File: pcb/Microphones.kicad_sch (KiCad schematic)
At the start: 38 parts, among them U4 AD8426ACPZ-R7, U5 AD8426ACPZ-R7

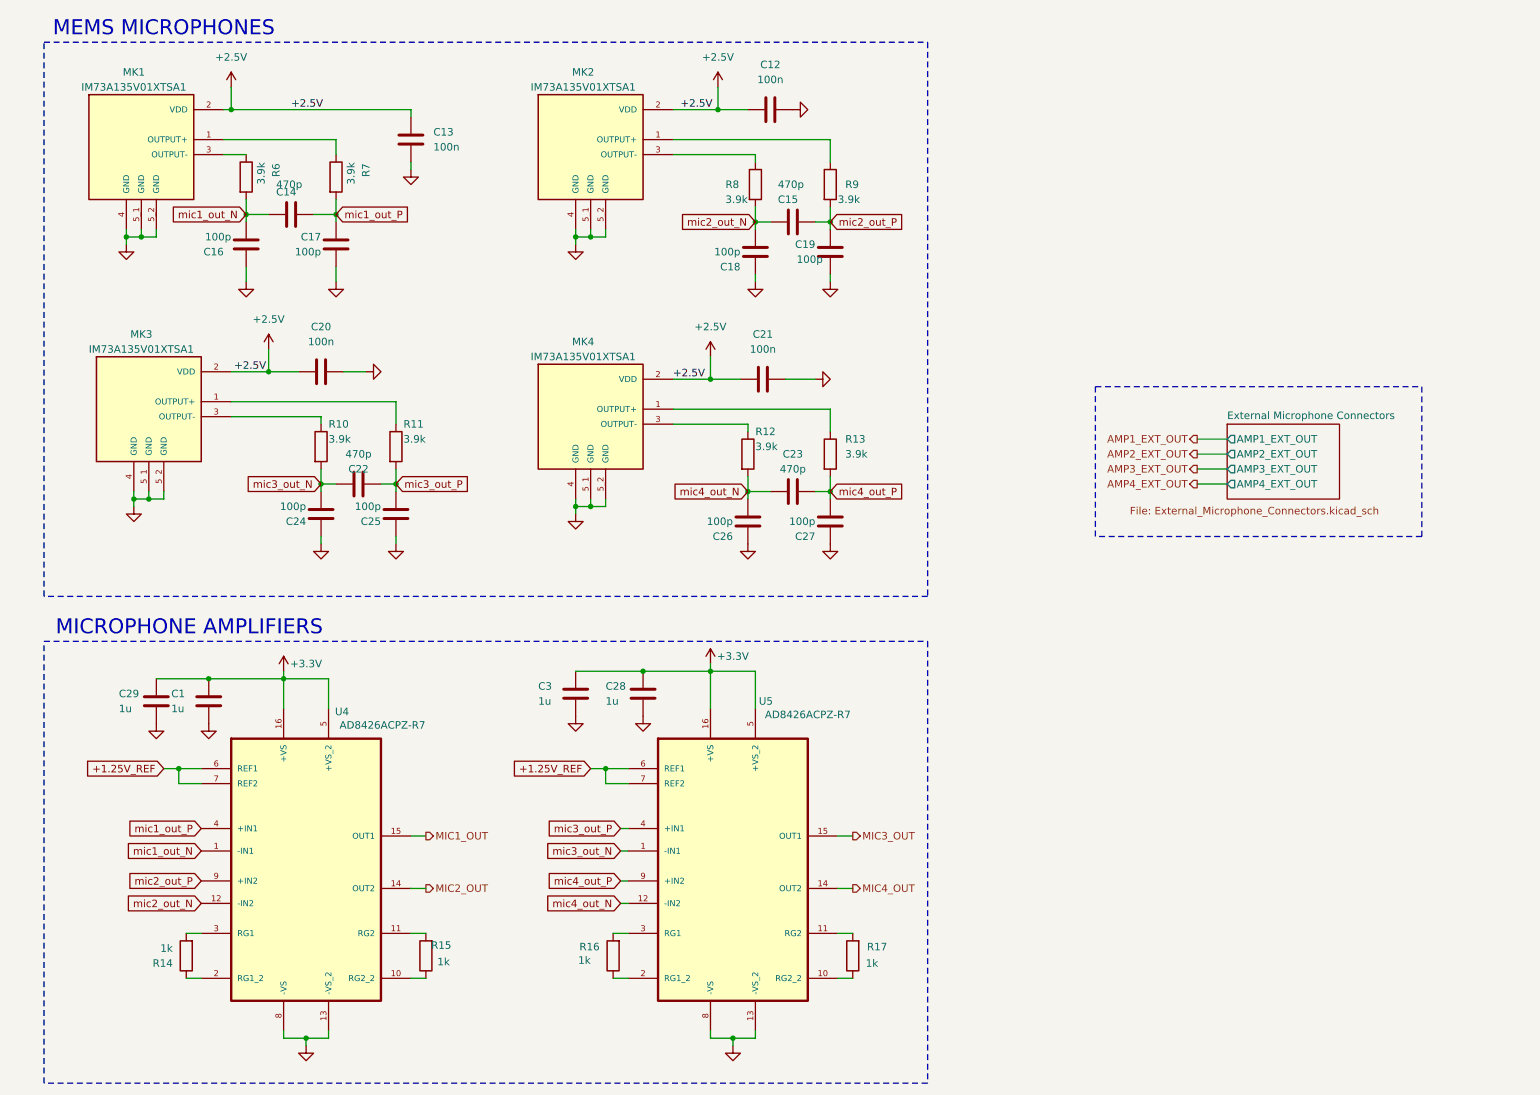
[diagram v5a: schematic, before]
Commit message: feat: Improve PCB design after tests of rev 0.8
- Added new generation of humidity sensor
- New silkscreen information for different components
- Added additional testpoints
- Removed PWM path for ultrasound transmitter
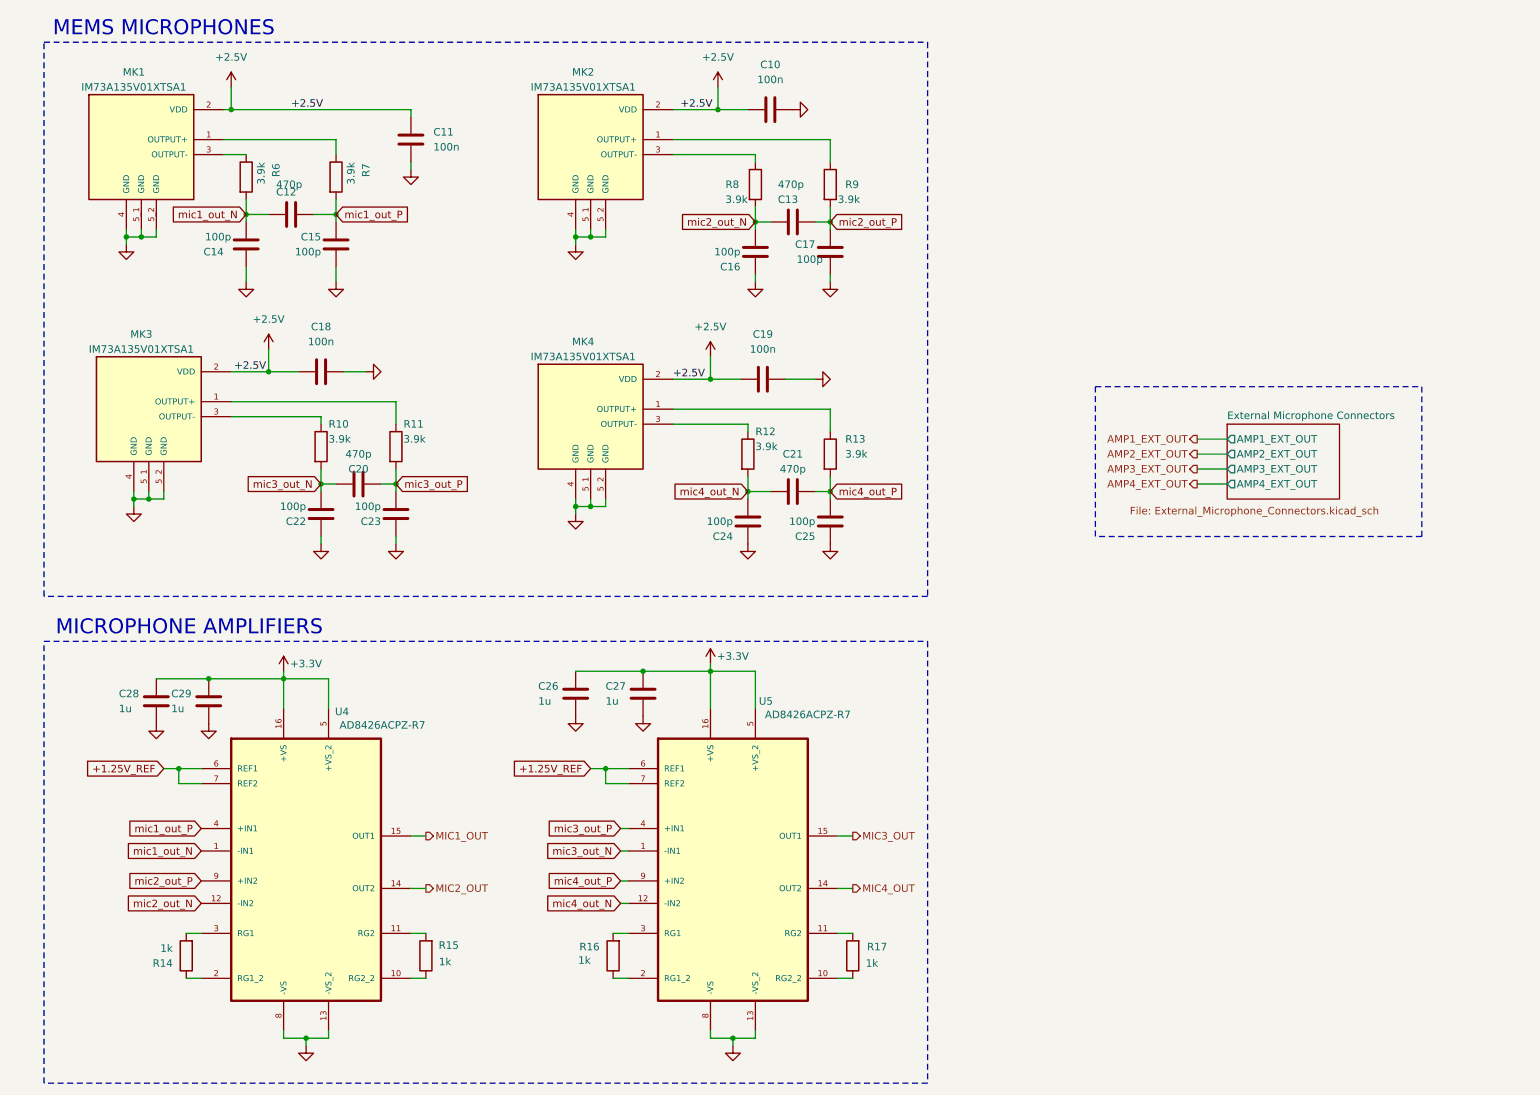
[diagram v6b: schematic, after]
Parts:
- C10: renamed from C12; footprint Capacitor_SMD:C_0603_1608Metric -> SensEdu:C_0603_1608Metric
- C11: renamed from C13; footprint Capacitor_SMD:C_0603_1608Metric -> SensEdu:C_0603_1608Metric
- C12: renamed from C14; footprint Capacitor_SMD:C_0603_1608Metric -> SensEdu:C_0603_1608Metric
- C13: renamed from C15; footprint Capacitor_SMD:C_0603_1608Metric -> SensEdu:C_0603_1608Metric
- C14: renamed from C16; footprint Capacitor_SMD:C_0603_1608Metric -> SensEdu:C_0603_1608Metric
- C15: renamed from C17; footprint Capacitor_SMD:C_0603_1608Metric -> SensEdu:C_0603_1608Metric
- C16: renamed from C18; footprint Capacitor_SMD:C_0603_1608Metric -> SensEdu:C_0603_1608Metric
- C17: renamed from C19; footprint Capacitor_SMD:C_0603_1608Metric -> SensEdu:C_0603_1608Metric
- C18: renamed from C20; footprint Capacitor_SMD:C_0603_1608Metric -> SensEdu:C_0603_1608Metric
- C19: renamed from C21; footprint Capacitor_SMD:C_0603_1608Metric -> SensEdu:C_0603_1608Metric
- C20: renamed from C22; footprint Capacitor_SMD:C_0603_1608Metric -> SensEdu:C_0603_1608Metric
- C21: renamed from C23; footprint Capacitor_SMD:C_0603_1608Metric -> SensEdu:C_0603_1608Metric
- C22: renamed from C24; footprint Capacitor_SMD:C_0603_1608Metric -> SensEdu:C_0603_1608Metric
- C23: renamed from C25; footprint Capacitor_SMD:C_0603_1608Metric -> SensEdu:C_0603_1608Metric
- C24: renamed from C26; footprint Capacitor_SMD:C_0603_1608Metric -> SensEdu:C_0603_1608Metric
- C25: renamed from C27; footprint Capacitor_SMD:C_0603_1608Metric -> SensEdu:C_0603_1608Metric
- C26: renamed from C3; footprint Capacitor_SMD:C_0603_1608Metric -> SensEdu:C_0603_1608Metric
- C27: renamed from C28; footprint Capacitor_SMD:C_0603_1608Metric -> SensEdu:C_0603_1608Metric
- C28: renamed from C29; footprint Capacitor_SMD:C_0603_1608Metric -> SensEdu:C_0603_1608Metric
- C29: renamed from C1; footprint Capacitor_SMD:C_0603_1608Metric -> SensEdu:C_0603_1608Metric
- R10, R11, R12, R13, R14, R15, R16, R17, R6, R7, R8, R9: footprint Resistor_SMD:R_0603_1608Metric -> SensEdu:R_0603_1608Metric

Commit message: refactor: Remove unnecessary comments
- Regenerate schematics
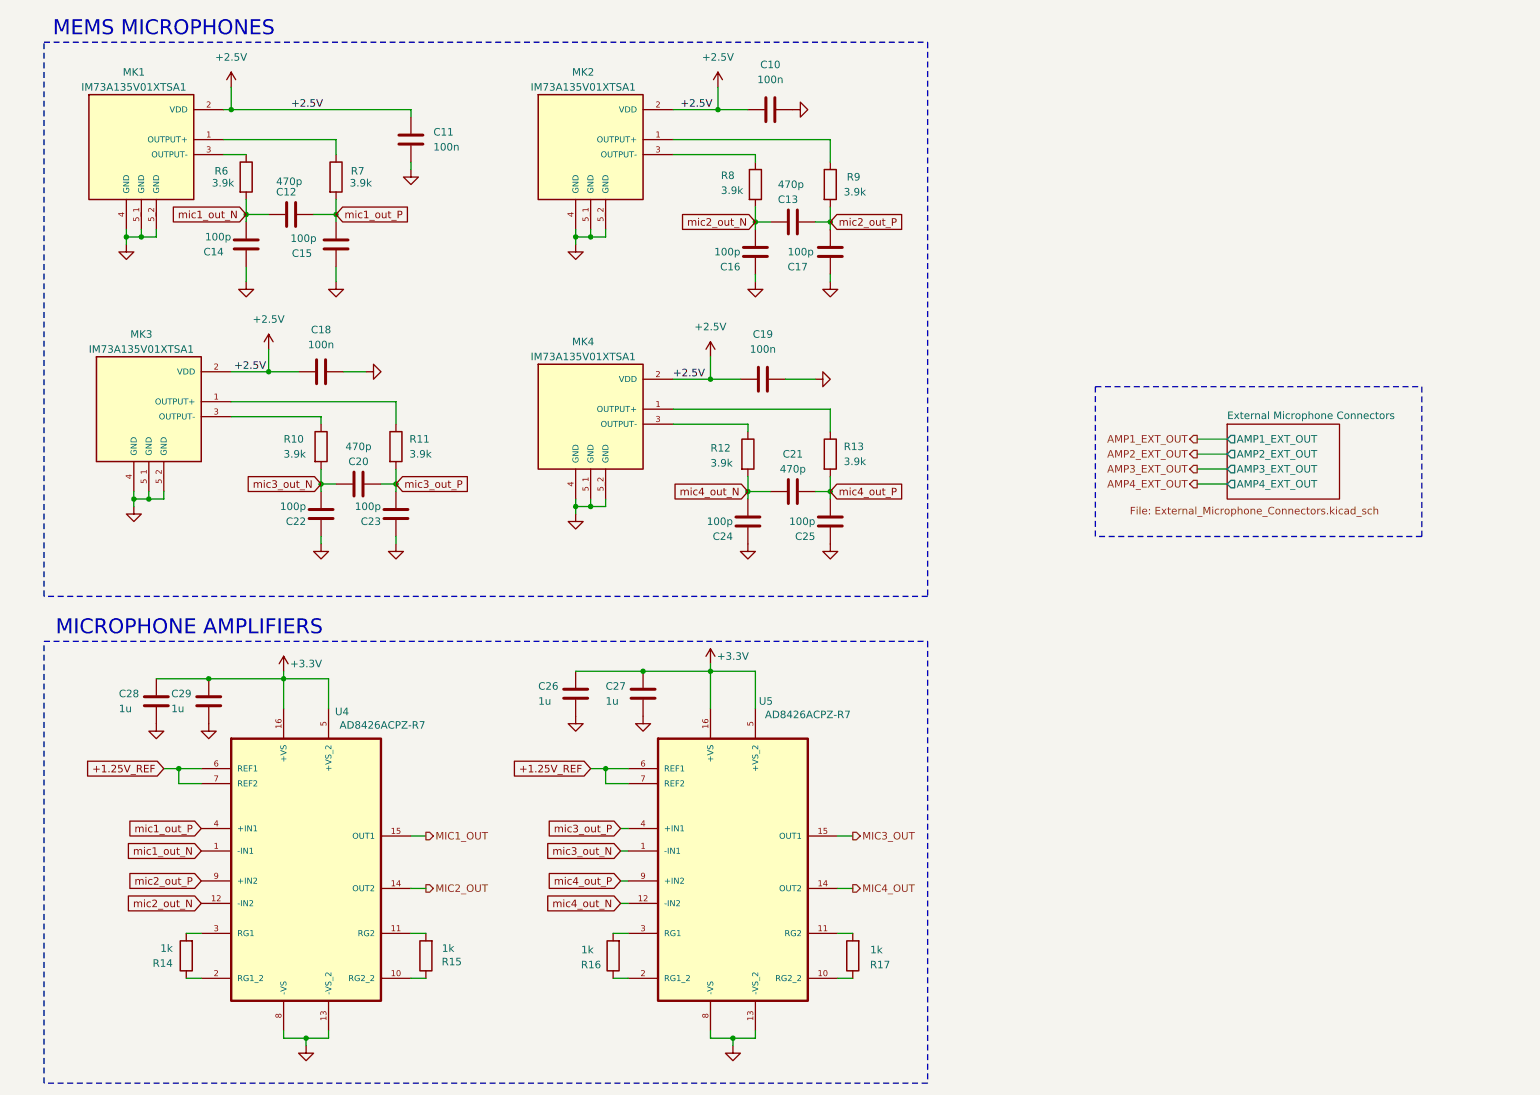
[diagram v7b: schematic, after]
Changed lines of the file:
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@@
 		(dnp no)
 		(property "Reference" "R15"
-			(at 93.218 170.942 0)
+			(at 93.726 173.736 0)
 			(effects
 				(font
@@
 		)
 		(property "Value" "1k"
-			(at 91.948 173.736 0)
+			(at 92.456 171.45 0)
 			(effects
 				(font
@@
 		(dnp no)
 		(property "Reference" "R8"
-			(at 138.43 41.91 0)
+			(at 137.668 40.386 0)
 			(effects
 				(font
@@
 		)
 		(property "Value" "3.9k"
-			(at 138.43 44.45 0)
+			(at 137.668 42.926 0)
 			(effects
 				(font
@@
 		(dnp no)
 		(property "Reference" "R12"
-			(at 143.51 83.82 0)
+			(at 135.89 86.614 0)
 			(effects
 				(font
@@
 		)
 		(property "Value" "3.9k"
-			(at 143.51 86.36 0)
+			(at 135.89 89.154 0)
 			(effects
 				(font
@@
 		(dnp no)
 		(property "Reference" "R11"
-			(at 83.82 82.55 0)
+			(at 84.836 85.09 0)
 			(effects
 				(font
@@
 		)
 		(property "Value" "3.9k"
-			(at 83.82 85.09 0)
+			(at 84.836 87.63 0)
 			(effects
 				(font
@@
 		(dnp no)
 		(property "Reference" "R17"
-			(at 165.862 171.196 0)
+			(at 166.37 174.244 0)
 			(effects
 				(font
@@
 		)
 		(property "Value" "1k"
-			(at 164.338 173.99 0)
+			(at 165.1 171.704 0)
 			(effects
 				(font
@@
 		(dnp no)
 		(property "Reference" "R13"
-			(at 158.75 85.09 0)
+			(at 158.496 86.36 0)
 			(effects
 				(font
@@
 		)
 		(property "Value" "3.9k"
-			(at 158.75 87.63 0)
+			(at 158.496 88.9 0)
 			(effects
 				(font
@@
 		(dnp no)
 		(property "Reference" "R9"
-			(at 158.75 41.91 0)
+			(at 159.004 40.64 0)
 			(effects
 				(font
@@
 		)
 		(property "Value" "3.9k"
-			(at 157.48 44.45 0)
+			(at 158.496 43.18 0)
 			(effects
 				(font
@@
 		(dnp no)
 		(property "Reference" "R16"
-			(at 117.094 171.196 0)
+			(at 117.348 174.244 0)
 			(effects
 				(font
@@
 		)
 		(property "Value" "1k"
-			(at 115.57 173.482 0)
+			(at 116.078 171.704 0)
 			(effects
 				(font
@@
 		(dnp no)
 		(property "Reference" "C17"
-			(at 153.67 52.07 0)
+			(at 152.4 55.88 0)
 			(effects
 				(font
@@
 		)
 		(property "Value" "100p"
-			(at 154.94 54.61 0)
+			(at 153.416 53.34 0)
 			(effects
 				(font
@@
 		(on_board yes)
 		(dnp no)
-		(fields_autoplaced yes)
 		(property "Reference" "C18"
-			(at 69.85 66.04 90)
+			(at 69.85 66.548 90)
 			(effects
 				(font
@@
 		)
 		(property "Value" "100n"
-			(at 69.85 68.58 90)
+			(at 69.85 69.088 90)
 			(effects
 				(font
@@
 		(dnp no)
 		(property "Reference" "R6"
-			(at 62.23 40.64 90)
+			(at 54.102 39.624 0)
 			(effects
 				(font
 					(size 1.27 1.27)
 				)
-				(justify left)
+				(justify right)
 			)
 		)
 		(property "Value" "3.9k"
-			(at 59.69 41.91 90)
+			(at 55.118 41.656 0)
 			(effects
 				(font
 					(size 1.27 1.27)
 				)
-				(justify left)
+				(justify right)
 			)
 		)
@@
 		(dnp no)
 		(property "Reference" "R7"
-			(at 77.47 40.64 90)
+			(at 77.216 39.624 0)
 			(effects
 				(font
 					(size 1.27 1.27)
 				)
-				(justify left)
+				(justify right)
 			)
 		)
 		(property "Value" "3.9k"
-			(at 74.93 41.91 90)
+			(at 78.486 41.656 0)
 			(effects
 				(font
 					(size 1.27 1.27)
 				)
-				(justify left)
+				(justify right)
 			)
 		)
@@
 		(dnp no)
 		(property "Reference" "C15"
-			(at 69.85 50.8 0)
+			(at 68.326 53.594 0)
 			(effects
 				(font
@@
 		)
 		(property "Value" "100p"
-			(at 69.85 53.34 0)
+			(at 69.088 51.054 0)
 			(effects
 				(font
@@
 		(dnp no)
 		(property "Reference" "R10"
-			(at 71.12 82.55 0)
+			(at 63.5 85.09 0)
 			(effects
 				(font
@@
 		)
 		(property "Value" "3.9k"
-			(at 71.12 85.09 0)
+			(at 63.5 87.63 0)
 			(effects
 				(font
@@
 		)
 		(property "Value" "470p"
-			(at 62.23 41.91 90)
+			(at 62.23 41.402 90)
 			(effects
 				(font
@@
 		(dnp no)
 		(property "Reference" "C20"
-			(at 76.2 90.17 90)
+			(at 76.2 88.9 90)
 			(effects
 				(font
@@
 		)
 		(property "Value" "470p"
-			(at 76.2 87.63 90)
+			(at 76.2 86.36 90)
 			(effects
 				(font
